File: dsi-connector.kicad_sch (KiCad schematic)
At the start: 12 parts, among them J1 Plug_Molex_SlimStack_2x20_556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

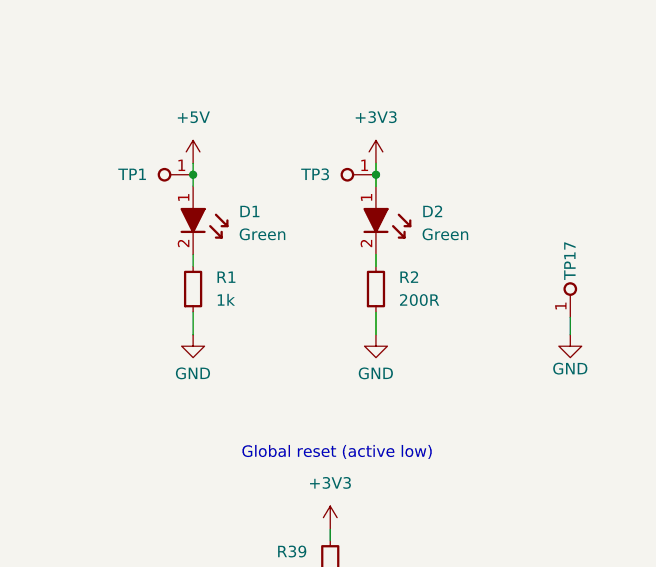
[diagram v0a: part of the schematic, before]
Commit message: [#58170] LED related improvements
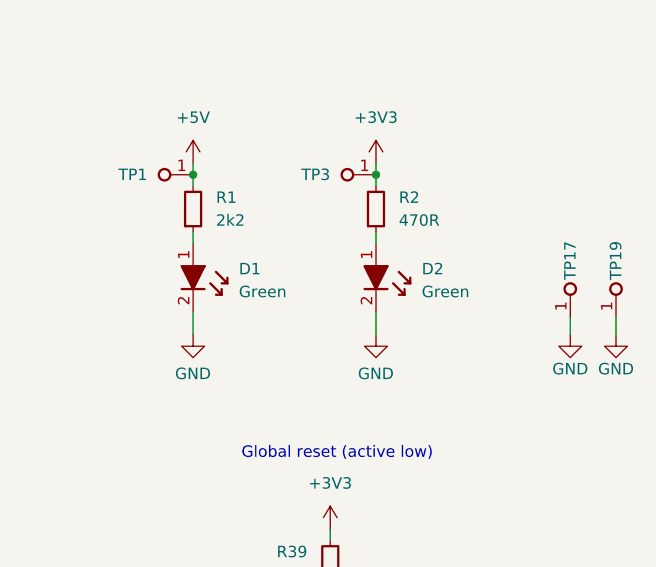
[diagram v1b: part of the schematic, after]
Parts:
- added TP19: TP_0.75mm_SMD, antmicro-footprints:TP_SMD_0.75mm, symbol antmicroTestPoints:TP_0.75mm_SMD
- R1: value R_1k_0402 -> R_2k2_0402; symbol antmicroResistors0402:R_1k_0402 -> antmicroResistors0402:R_2k2_0402; MPN CR0402-FX-1001GLF -> CR0402-FX-2201GLF; Val 1k -> 2k2
- R2: value R_200R_0402 -> R_470R_0402; symbol antmicroResistors0402:R_200R_0402 -> antmicroResistors0402:R_470R_0402; MPN CR0402-FX-2000GLF -> CR0402-FX-4700GLF; Val 200R -> 470R
- TP1, TP3: value TP_1mm_SMD -> TP_0.75mm_SMD; footprint antmicro-footprints:TP_SMD_1mm -> antmicro-footprints:TP_SMD_0.75mm; symbol antmicroTestPoints:TP_1mm_SMD -> antmicroTestPoints:TP_0.75mm_SMD; now left out of the parts list
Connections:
- net +3V3: now also R2.2; no longer D2.1
- net +5V: now also R1.2; no longer D1.1
- net GND: now also D1.2, D2.2, TP19.1; no longer R1.1, R2.1
- new net: D2.1, R2.1
- new net: D1.1, R1.1
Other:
- moved on the sheet: D1, D2, R1, R2
